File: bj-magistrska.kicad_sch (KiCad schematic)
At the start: 3 parts, among them J1 Screw_Terminal_01x02, J2 20 pos, J3 Screw_Terminal_01x02

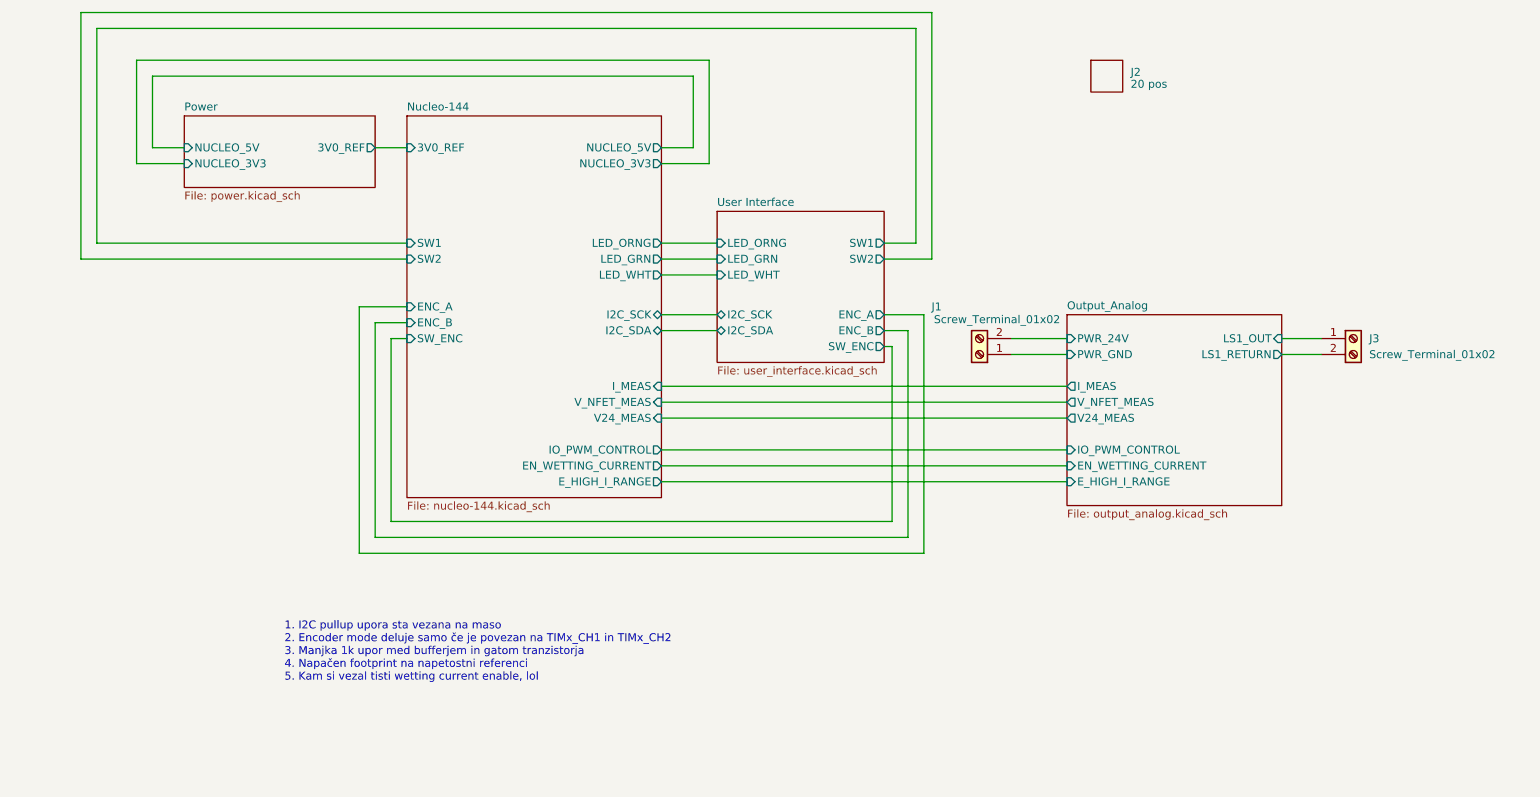
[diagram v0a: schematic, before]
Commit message: - Removed I2C lines - Added mission resistor between buffer and transistor gate - Removed wetting current & high range enable - Added ILI9341 TFT LCD - Removed OLED - Upped current gain to ~100
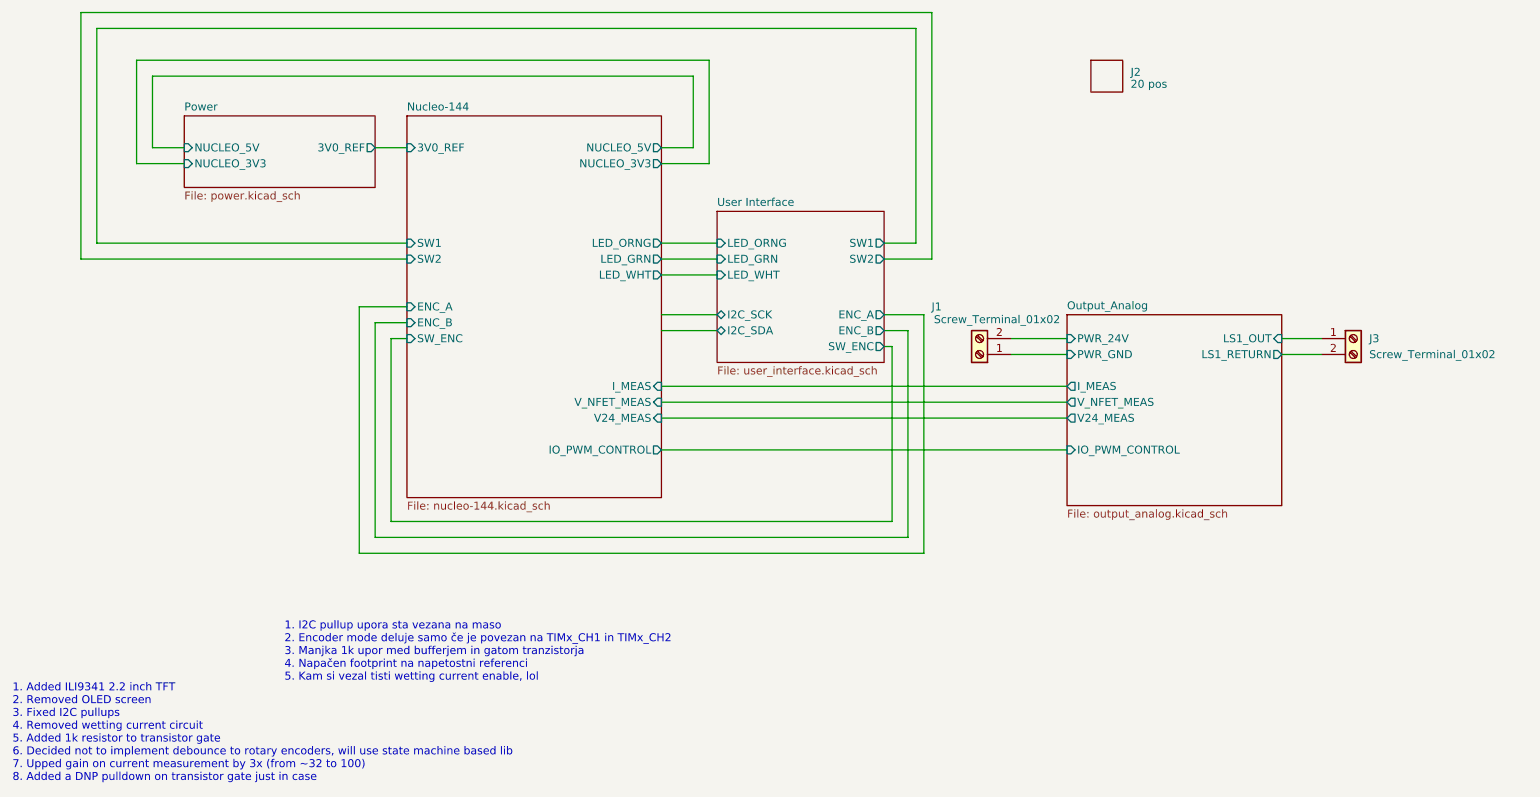
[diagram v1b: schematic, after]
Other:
- sheet Nucleo-144 ports: added none; removed EN_WETTING_CURRENT, E_HIGH_I_RANGE, I2C_SCK, I2C_SDA
- sheet Output_Analog ports: added none; removed EN_WETTING_CURRENT, E_HIGH_I_RANGE
- note added: "1. Added ILI9341 2.2 inch TFT 2. Removed OLED screen 3. Fixed I2C pullups 4. Removed wetting current circuit 5. Added 1k resistor to transistor gate 6. Decided not to implement debounce to rotary encoders, will use state machine based lib 7. Upped gain on current measurement by 3x (from ~32 to 100) 8. Added a DNP pulldown on transistor gate just in case"
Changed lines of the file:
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@@
-	(wire
-		(pts
-			(xy 130.81 137.16) (xy 195.58 137.16)
-		)
-		(stroke
-			(width 0)
-			(type default)
-		)
-	)
 	(wire
 		(pts
@@
 	(wire
 		(pts
-			(xy 130.81 134.62) (xy 195.58 134.62)
-		)
-		(stroke
-			(width 0)
-			(type default)
-		)
-	)
-	(wire
-		(pts
 			(xy 186.69 114.3) (xy 195.58 114.3)
 		)
@@
 			(width 0)
 			(type default)
+		)
+	)
+	(text "1. Added ILI9341 2.2 inch TFT\n2. Removed OLED screen\n3. Fixed I2C pullups\n4. Removed wetting current circuit\n5. Added 1k resistor to transistor gate\n6. Decided not to implement debounce to rotary encoders, will use state machine based lib\n7. Upped gain on current measurement by 3x (from ~32 to 100)\n8. Added a DNP pulldown on transistor gate just in case"
+		(exclude_from_sim no)
+		(at 27.178 177.292 0)
+		(effects
+			(font
+				(size 1.27 1.27)
+			)
+			(justify left)
 		)
 	)
@@
 			)
 		)
-		(pin "I2C_SCK" bidirectional
-			(at 130.81 110.49 0)
-			(effects
-				(font
-					(size 1.27 1.27)
-				)
-				(justify right)
-			)
-		)
-		(pin "I2C_SDA" bidirectional
-			(at 130.81 113.03 0)
-			(effects
-				(font
-					(size 1.27 1.27)
-				)
-				(justify right)
-			)
-		)
-		(pin "E_HIGH_I_RANGE" output
-			(at 130.81 137.16 0)
-			(effects
-				(font
-					(size 1.27 1.27)
-				)
-				(justify right)
-			)
-		)
-		(pin "EN_WETTING_CURRENT" output
-			(at 130.81 134.62 0)
-			(effects
-				(font
-					(size 1.27 1.27)
-				)
-				(justify right)
-			)
-		)
 		(pin "IO_PWM_CONTROL" output
 			(at 130.81 132.08 0)
@@
 			)
 		)
-		(pin "E_HIGH_I_RANGE" input
-			(at 195.58 137.16 180)
-			(effects
-				(font
-					(size 1.27 1.27)
-				)
-				(justify left)
-			)
-		)
 		(pin "IO_PWM_CONTROL" input
 			(at 195.58 132.08 180)
 			(effects
 				(font
-					(size 1.27 1.27)
-				)
-				(justify left)
-			)
-		)
-		(pin "EN_WETTING_CURRENT" input
-			(at 195.58 134.62 180)
-			(effects
-				(font
